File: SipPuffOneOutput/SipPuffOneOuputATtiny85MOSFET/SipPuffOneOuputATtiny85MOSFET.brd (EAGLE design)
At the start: 48 x 70 mm, 13 parts, among them U1 ATTINY85-20PU, U2 4936BM08A-M

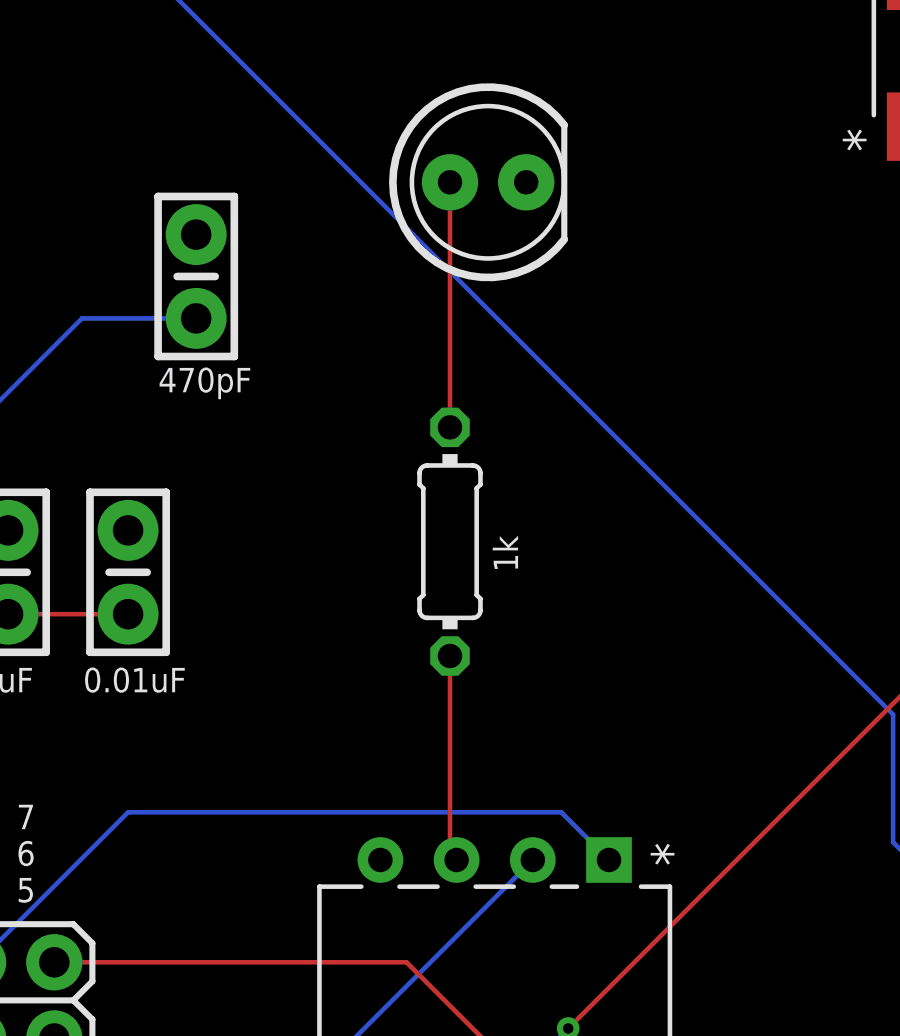
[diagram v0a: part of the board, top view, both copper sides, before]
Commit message: Changed resistors size
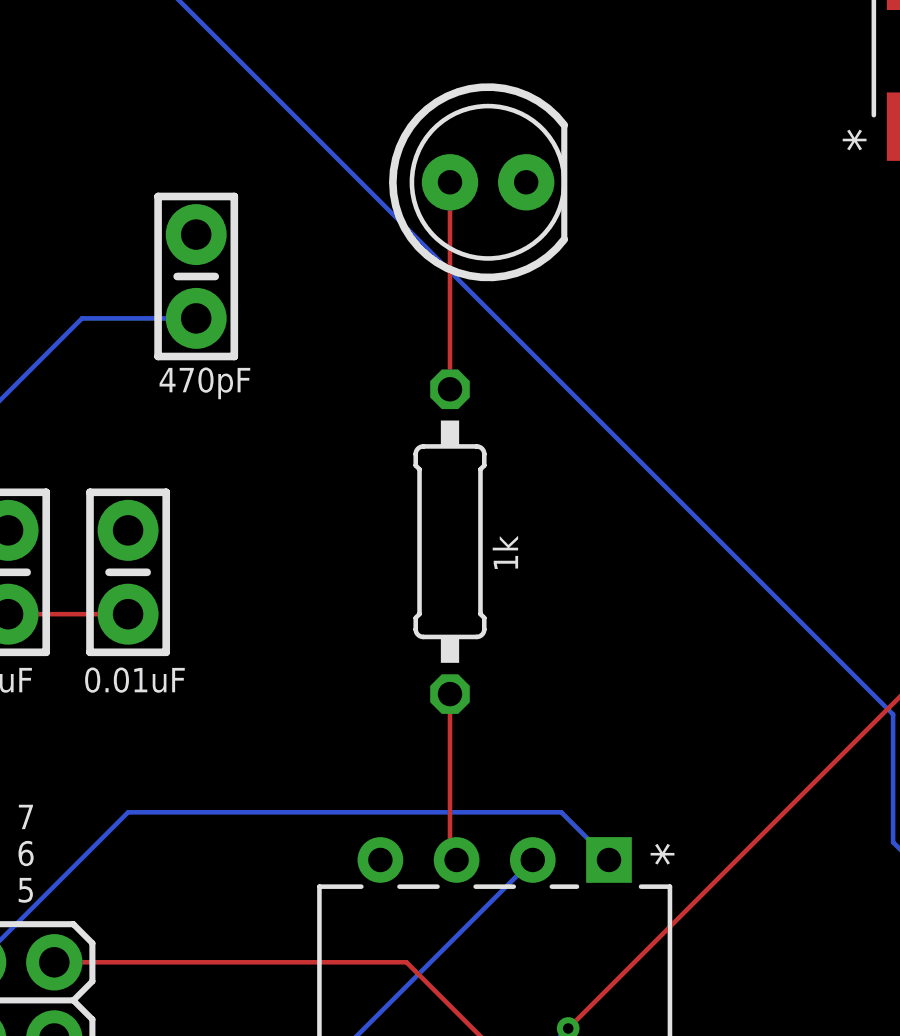
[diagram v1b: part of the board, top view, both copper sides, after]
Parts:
- R1: device MMC Eagle:RESISTOR_0204/7 -> MMC Eagle:RESISTOR_0207/10
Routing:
- net N$5: track 8.17 -> 6.90 mm
- net N$4: track 6.89 -> 5.62 mm
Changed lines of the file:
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@@
 <drawing>
 <settings>
-<setting alwaysvectorfont="yes"/>
+<setting alwaysvectorfont="no"/>
 <setting verticaltext="up"/>
 </settings>
@@
 <attribute name="VALUE" x="20.444" y="14.89" size="1.27" layer="27"/>
 </element>
-<element name="R1" library="MMC Eagle" library_urn="urn:adsk.eagle:library:3491419" package="RESISTOR_0204/7" package3d_urn="urn:adsk.eagle:package:3491542/2" value="" x="22.73" y="38.02" smashed="yes" rot="R270">
+<element name="R1" library="MMC Eagle" library_urn="urn:adsk.eagle:library:3491419" package="RESISTOR_0207/10" package3d_urn="urn:adsk.eagle:package:5426338/2" value="" x="22.73" y="38.02" smashed="yes" rot="R270">
 <attribute name="VALUE" x="22.2474" y="39.6456" size="0.9906" layer="27" ratio="10" rot="R270"/>
 </element>
@@
 <contactref element="U1" pad="3"/>
 <contactref element="R1" pad="2"/>
-<wire x1="22.73" y1="34.21" x2="22.73" y2="27.63" width="0.1524" layer="1"/>
+<wire x1="22.73" y1="32.94" x2="22.73" y2="27.63" width="0.1524" layer="1"/>
 <wire x1="22.73" y1="27.63" x2="22.95" y2="27.41" width="0.1524" layer="1"/>
 </signal>
@@
 <contactref element="R1" pad="1"/>
 <contactref element="D1" pad="A"/>
-<wire x1="22.73" y1="50" x2="22.73" y2="41.83" width="0.1524" layer="1"/>
+<wire x1="22.73" y1="50" x2="22.73" y2="43.1" width="0.1524" layer="1"/>
 </signal>
 <signal name="GND">
